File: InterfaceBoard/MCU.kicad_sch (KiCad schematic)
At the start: 6 parts, among them J1 Conn_ARM_JTAG_SWD_10, U4 STM32G0B1RET

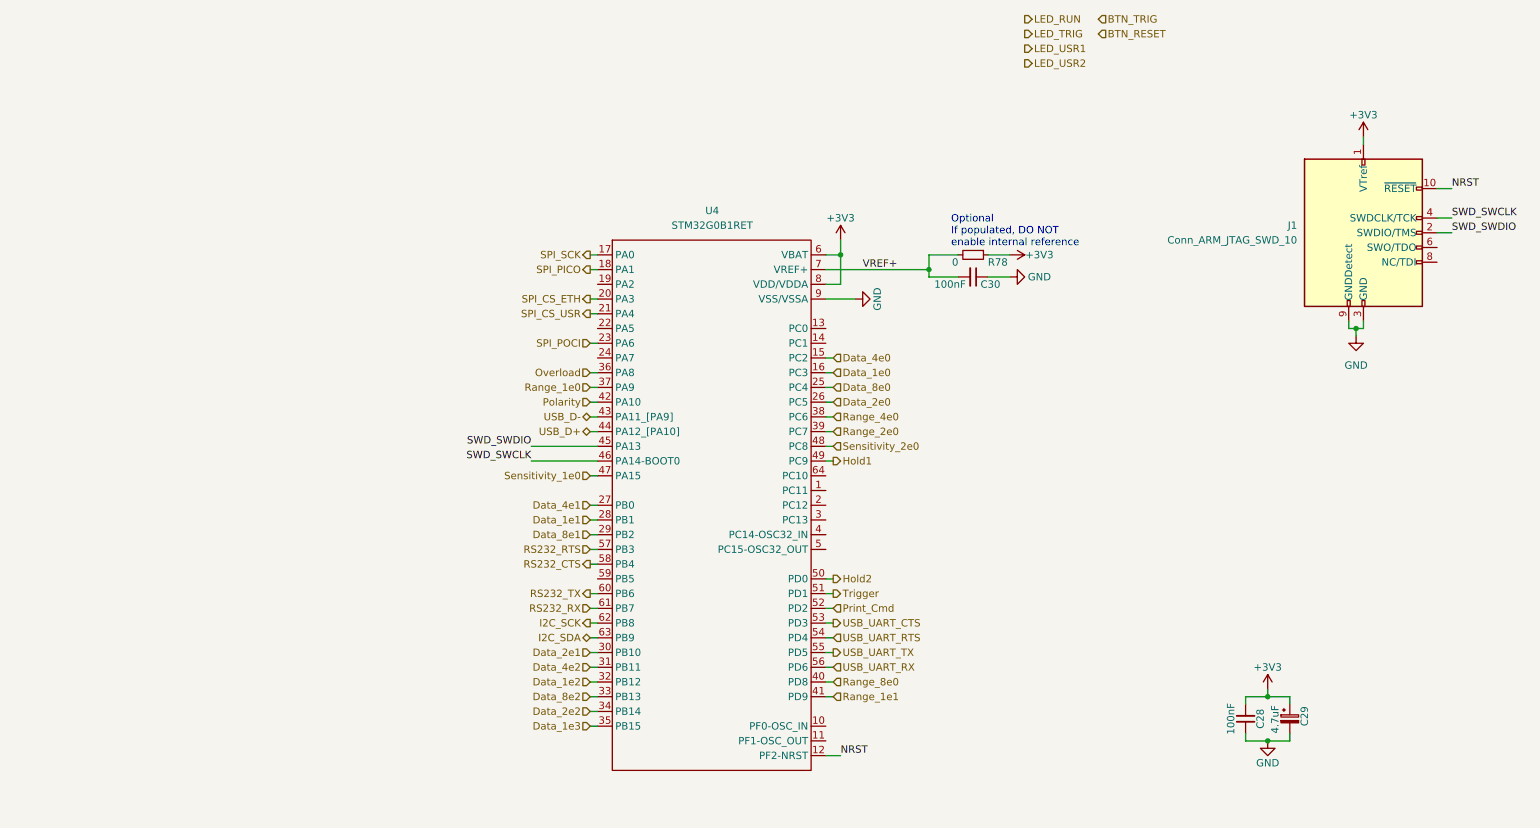
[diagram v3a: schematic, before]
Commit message: InterfaceBoard: Update connector footprint
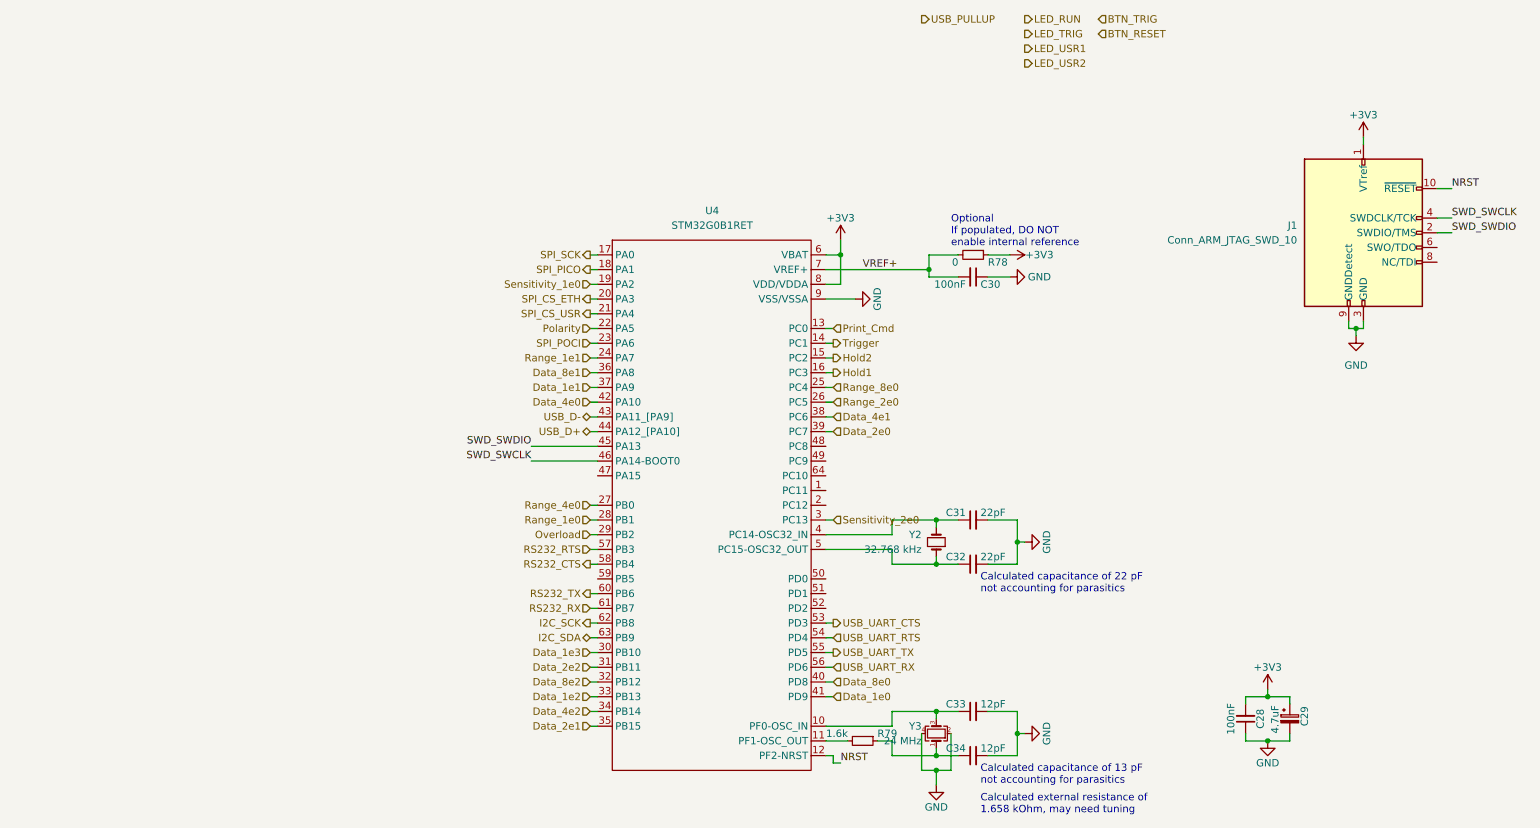
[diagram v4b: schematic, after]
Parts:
- added C31, C32: 22pF, Capacitor_SMD:C_0603_1608Metric, symbol Device:C_Small
- added C33, C34: 12pF, Capacitor_SMD:C_0603_1608Metric, symbol Device:C_Small
- added R79: 1.6k, Resistor_SMD:R_0603_1608Metric, symbol Device:R_Small
- added Y2: 32.768 kHz, Crystal:Crystal_C26-LF_D2.1mm_L6.5mm_Horizontal, symbol Device:Crystal_Small
- added Y3: 24 MHz, Crystal:Crystal_SMD_3225-4Pin_3.2x2.5mm, symbol Device:Crystal_GND24_Small
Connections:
- net Data_1e0: now also U4.41 (PD9); no longer U4.16 (PC3)
- net Data_1e1: now also U4.37 (PA9); no longer U4.28 (PB1)
- net Data_1e2: now also U4.33 (PB13); no longer U4.32 (PB12)
- net Data_1e3: now also U4.30 (PB10); no longer U4.35 (PB15)
- net Data_2e0: now also U4.39 (PC7); no longer U4.26 (PC5)
- net Data_2e1: now also U4.35 (PB15); no longer U4.30 (PB10)
- net Data_2e2: now also U4.31 (PB11); no longer U4.34 (PB14)
- net Data_4e0: now also U4.42 (PA10); no longer U4.15 (PC2)
- net Data_4e1: now also U4.38 (PC6); no longer U4.27 (PB0)
- net Data_4e2: now also U4.34 (PB14); no longer U4.31 (PB11)
- net Data_8e0: now also U4.40 (PD8); no longer U4.25 (PC4)
- net Data_8e1: now also U4.36 (PA8); no longer U4.29 (PB2)
- net Data_8e2: now also U4.32 (PB12); no longer U4.33 (PB13)
- net GND: now also C31.2, C32.2, C33.2, C34.2, Y3.2, Y3.4
- net Hold1: now also U4.16 (PC3); no longer U4.49 (PC9)
- net Hold2: now also U4.15 (PC2); no longer U4.50 (PD0)
- net Overload: now also U4.29 (PB2); no longer U4.36 (PA8)
- net Polarity: now also U4.22 (PA5); no longer U4.42 (PA10)
- net Print_Cmd: now also U4.13 (PC0); no longer U4.52 (PD2)
- net Range_1e0: now also U4.28 (PB1); no longer U4.37 (PA9)
- net Range_1e1: now also U4.24 (PA7); no longer U4.41 (PD9)
- net Range_2e0: now also U4.26 (PC5); no longer U4.39 (PC7)
- net Range_4e0: now also U4.27 (PB0); no longer U4.38 (PC6)
- net Range_8e0: now also U4.25 (PC4); no longer U4.40 (PD8)
- net Sensitivity_1e0: now also U4.19 (PA2); no longer U4.47 (PA15)
- net Sensitivity_2e0: now also U4.3 (PC13); no longer U4.48 (PC8)
- net Trigger: now also U4.14 (PC1); no longer U4.51 (PD1)
- net at U4.10 (PF0-OSC_IN): now also C33.1, Y3.3
- net at U4.11 (PF1-OSC_OUT): now also R79.2
- net at U4.4 (PC14-OSC32_IN): now also C31.1, Y2.2
- net at U4.5 (PC15-OSC32_OUT): now also C32.1, Y2.1
- new net: C34.1, R79.1, Y3.1
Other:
- note added: "Calculated capacitance of 13 pF not accounting for parasitics"
- note added: "Calculated capacitance of 22 pF not accounting for parasitics"
- note added: "Calculated external resistance of 1.658 kOhm, may need tuning"

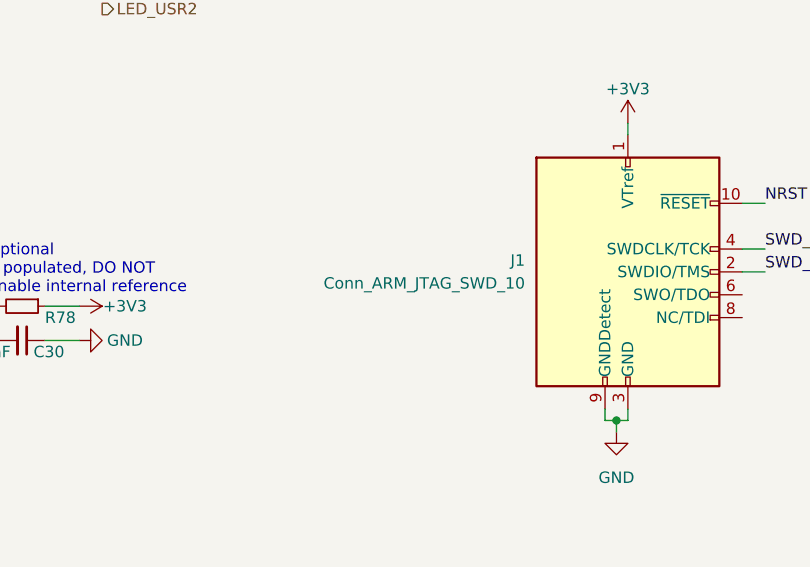
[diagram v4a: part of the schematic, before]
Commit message: InterfaceBoard: Add 3.3 V regulater, test points.
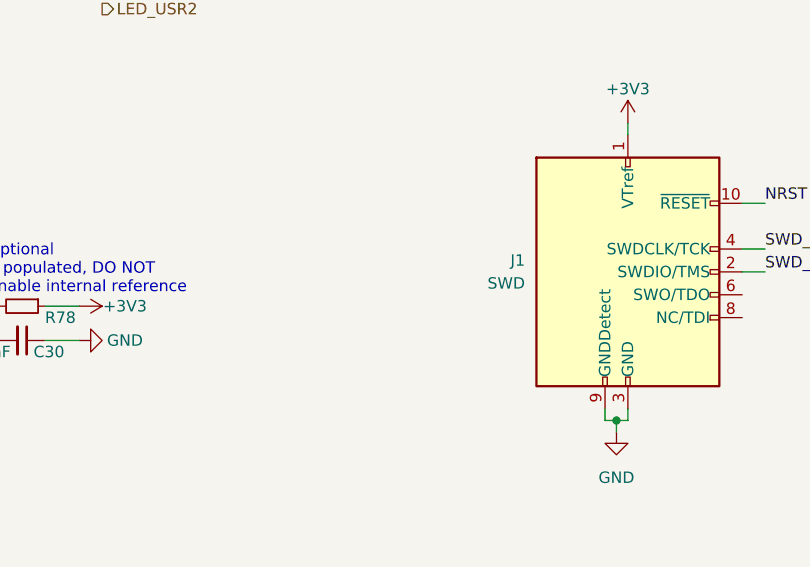
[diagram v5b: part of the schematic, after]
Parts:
- J1: value Conn_ARM_JTAG_SWD_10 -> SWD
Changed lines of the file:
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@@
       (effects (font (size 1.27 1.27)) (justify right))
     )
-    (property "Value" "Conn_ARM_JTAG_SWD_10" (id 1) (at 237.49 54.6099 0)
+    (property "Value" "SWD" (id 1) (at 237.49 54.6099 0)
       (effects (font (size 1.27 1.27)) (justify right))
     )

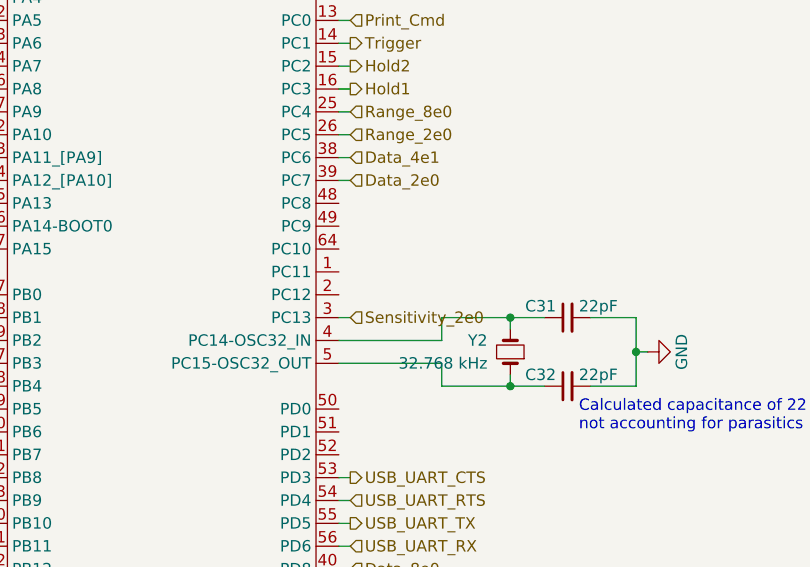
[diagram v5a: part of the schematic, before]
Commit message: InterfaceBoard: Routed some digital interfaces to MCU
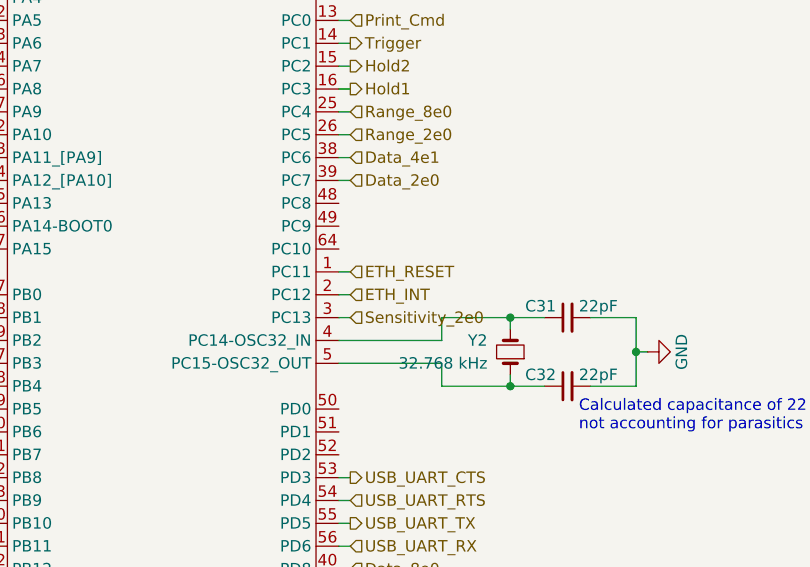
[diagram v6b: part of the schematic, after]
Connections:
- net ETH_RESET: now reaches U4.1 (PC11)
- net ETH_INT: now reaches U4.2 (PC12)
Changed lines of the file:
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@@
+    (stroke (width 0) (type default) (color 0 0 0 0))
+  )
+  (wire (pts (xy 156.21 100.33) (xy 157.48 100.33))
     (stroke (width 0) (type default) (color 0 0 0 0))
   )
@@
   )
   (wire (pts (xy 189.23 110.49) (xy 184.15 110.49))
+    (stroke (width 0) (type default) (color 0 0 0 0))
+  )
+  (wire (pts (xy 156.21 97.79) (xy 157.48 97.79))
     (stroke (width 0) (type default) (color 0 0 0 0))
   )
@@
     (effects (font (size 1.27 1.27)) (justify left))
   )
+  (hierarchical_label "ETH_RESET" (shape input) (at 157.48 97.79 0)
+    (effects (font (size 1.27 1.27)) (justify left))
+  )
   (hierarchical_label "Range_1e0" (shape input) (at 115.57 102.87 180)
     (effects (font (size 1.27 1.27)) (justify right))
@@
     (effects (font (size 1.27 1.27)) (justify left))
   )
+  (hierarchical_label "ETH_INT" (shape input) (at 157.48 100.33 0)
+    (effects (font (size 1.27 1.27)) (justify left))
+  )

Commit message: InterfaceBoard: Place and route buttons and LEDs.
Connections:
- net NRST is gone; now on net BTN_RESET: J1.10 (~{RESET}), U4.12 (PF2-NRST)
- net BTN_TRIG: now also U4.64 (PC10)
- net LED_RUN: now also U4.47 (PA15)
- net LED_TRIG: now also U4.48 (PC8)
- net LED_USR1: now also U4.49 (PC9)
- net LED_USR2: now also U4.50 (PD0)
- net USB_PULLUP: now also U4.59 (PB5)
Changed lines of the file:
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@@
   (junction (at 175.26 146.05) (diameter 0) (color 0 0 0 0)
   )
+  (junction (at 157.48 144.78) (diameter 0) (color 0 0 0 0)
+  )
   (junction (at 247.65 69.85) (diameter 0) (color 0 0 0 0)
   )
@@
     (stroke (width 0) (type default) (color 0 0 0 0))
   )
+  (wire (pts (xy 156.21 113.03) (xy 157.48 113.03))
+    (stroke (width 0) (type default) (color 0 0 0 0))
+  )
   (wire (pts (xy 105.41 90.17) (xy 116.84 90.17))
     (stroke (width 0) (type default) (color 0 0 0 0))
   )
+  (wire (pts (xy 115.57 113.03) (xy 116.84 113.03))
+    (stroke (width 0) (type default) (color 0 0 0 0))
+  )
   (wire (pts (xy 189.23 135.89) (xy 189.23 139.7))
     (stroke (width 0) (type default) (color 0 0 0 0))
@@
     (stroke (width 0) (type default) (color 0 0 0 0))
   )
+  (wire (pts (xy 156.21 95.25) (xy 157.48 95.25))
+    (stroke (width 0) (type default) (color 0 0 0 0))
+  )
   (wire (pts (xy 167.64 143.51) (xy 175.26 143.51))
     (stroke (width 0) (type default) (color 0 0 0 0))
@@
     (stroke (width 0) (type default) (color 0 0 0 0))
   )
+  (wire (pts (xy 158.75 147.32) (xy 157.48 147.32))
+    (stroke (width 0) (type default) (color 0 0 0 0))
+  )
   (wire (pts (xy 247.65 69.85) (xy 248.92 69.85))
     (stroke (width 0) (type default) (color 0 0 0 0))
@@
     (stroke (width 0) (type default) (color 0 0 0 0))
   )
+  (wire (pts (xy 156.21 90.17) (xy 157.48 90.17))
+    (stroke (width 0) (type default) (color 0 0 0 0))
+  )
+  (wire (pts (xy 115.57 95.25) (xy 116.84 95.25))
+    (stroke (width 0) (type default) (color 0 0 0 0))
+  )
   (wire (pts (xy 115.57 67.31) (xy 116.84 67.31))
     (stroke (width 0) (type default) (color 0 0 0 0))
@@
   )
   (wire (pts (xy 177.8 146.05) (xy 175.26 146.05))
+    (stroke (width 0) (type default) (color 0 0 0 0))
+  )
+  (wire (pts (xy 156.21 92.71) (xy 157.48 92.71))
+    (stroke (width 0) (type default) (color 0 0 0 0))
+  )
+  (wire (pts (xy 157.48 147.32) (xy 157.48 144.78))
     (stroke (width 0) (type default) (color 0 0 0 0))
   )
@@
     (effects (font (size 1.27 1.27)) (justify right))
   )
-  (hierarchical_label "LED_USR2" (shape output) (at 190.5 24.13 0)
+  (hierarchical_label "LED_USR2" (shape output) (at 157.48 113.03 0)
     (effects (font (size 1.27 1.27)) (justify left))
   )
@@
     (effects (font (size 1.27 1.27)) (justify left))
   )
-  (hierarchical_label "LED_RUN" (shape output) (at 190.5 16.51 0)
-    (effects (font (size 1.27 1.27)) (justify left))
+  (hierarchical_label "LED_RUN" (shape output) (at 115.57 95.25 180)
+    (effects (font (size 1.27 1.27)) (justify right))
   )
   (hierarchical_label "Data_1e3" (shape input) (at 115.57 125.73 180)
@@
     (effects (font (size 1.27 1.27)) (justify left))
   )
+  (hierarchical_label "USB_PULLUP" (shape output) (at 115.57 113.03 180)
+    (effects (font (size 1.27 1.27)) (justify right))
+  )
   (hierarchical_label "USB_UART_RX" (shape input) (at 157.48 128.27 0)
     (effects (font (size 1.27 1.27)) (justify left))
@@
     (effects (font (size 1.27 1.27)) (justify right))
   )
-  (hierarchical_label "USB_PULLUP" (shape output) (at 172.72 16.51 0)
-    (effects (font (size 1.27 1.27)) (justify left))
-  )
   (hierarchical_label "Data_1e0" (shape input) (at 157.48 133.35 0)
     (effects (font (size 1.27 1.27)) (justify left))
@@
     (effects (font (size 1.27 1.27)) (justify right))
   )
-  (hierarchical_label "BTN_TRIG" (shape input) (at 203.2 16.51 0)
+  (hierarchical_label "BTN_TRIG" (shape input) (at 157.48 95.25 0)
     (effects (font (size 1.27 1.27)) (justify left))
   )
@@
     (effects (font (size 1.27 1.27)) (justify right))
   )
-  (hierarchical_label "BTN_RESET" (shape input) (at 203.2 19.05 0)
+  (hierarchical_label "BTN_RESET" (shape input) (at 158.75 147.32 0)
     (effects (font (size 1.27 1.27)) (justify left))
   )
@@
     (effects (font (size 1.27 1.27)) (justify right))
   )
-  (hierarchical_label "LED_TRIG" (shape output) (at 190.5 19.05 0)
+  (hierarchical_label "LED_TRIG" (shape output) (at 157.48 90.17 0)
     (effects (font (size 1.27 1.27)) (justify left))
   )
@@
     (effects (font (size 1.27 1.27)) (justify right))
   )
-  (hierarchical_label "LED_USR1" (shape output) (at 190.5 21.59 0)
-    (effects (font (size 1.27 1.27)) (justify left))
-  )
+  (hierarchical_label "LED_USR1" (shape output) (at 157.48 92.71 0)
+    (effects (font (size 1.27 1.27)) (justify left))
+  )

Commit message: InterfaceBoard: Rev 1.0
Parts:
- renumbered C33 to C10, C29 to C11, C31 to C30, C32 to C31, C28 to C32, C30 to C33, C34 to C9, J1 to J4, R79 to R16, R78 to R86, U4 to U2, Y3 to Y2, Y2 to Y3
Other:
- company: (none) -> Peter Farley
- title: (none) -> Kiethley 615 Interface Board
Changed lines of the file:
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@@
 (kicad_sch (version 20211123) (generator eeschema)
   (paper "A4")
+  (title_block
+    (title "Kiethley 615 Interface Board")
+    (date "2023-03-04")
+    (rev "1.0")
+    (company "Peter Farley")
+    (comment 1 "Rev 1.0: Initial revision")
+  )
   (junction (at 189.23 106.68) (diameter 0) (color 0 0 0 0)
   )
@@
   (symbol (lib_id "Device:C_Small") (at 181.61 60.96 270) (mirror x) (unit 1)
     (in_bom yes) (on_board yes)
-    (property "Reference" "C30" (id 0) (at 182.88 62.23 90)
+    (property "Reference" "C33" (id 0) (at 182.88 62.23 90)
       (effects (font (size 1.27 1.27)) (justify left))
     )
@@
   (symbol (lib_id "Device:C_Small") (at 181.61 143.51 90) (unit 1)
     (in_bom yes) (on_board yes)
-    (property "Reference" "C34" (id 0) (at 180.34 142.24 90)
+    (property "Reference" "C9" (id 0) (at 180.34 142.24 90)
       (effects (font (size 1.27 1.27)) (justify left))
     )
@@
   (symbol (lib_id "Device:C_Small") (at 181.61 102.87 90) (unit 1)
     (in_bom yes) (on_board yes)
-    (property "Reference" "C31" (id 0) (at 180.34 101.6 90)
+    (property "Reference" "C30" (id 0) (at 180.34 101.6 90)
       (effects (font (size 1.27 1.27)) (justify left))
     )
@@
   (symbol (lib_id "Device:R_Small") (at 181.61 57.15 270) (unit 1)
     (in_bom yes) (on_board yes)
-    (property "Reference" "R78" (id 0) (at 184.15 58.42 90)
+    (property "Reference" "R86" (id 0) (at 184.15 58.42 90)
       (effects (font (size 1.27 1.27)) (justify left))
     )
@@
   (symbol (lib_id "Device:Crystal_Small") (at 175.26 106.68 90) (unit 1)
     (in_bom yes) (on_board yes)
-    (property "Reference" "Y2" (id 0) (at 172.72 105.41 90)
+    (property "Reference" "Y3" (id 0) (at 172.72 105.41 90)
       (effects (font (size 1.27 1.27)) (justify left))
     )
@@
   (symbol (lib_id "Device:R_Small") (at 162.56 140.97 270) (unit 1)
     (in_bom yes) (on_board yes)
-    (property "Reference" "R79" (id 0) (at 165.1 139.7 90)
+    (property "Reference" "R16" (id 0) (at 165.1 139.7 90)
       (effects (font (size 1.27 1.27)) (justify left))
     )
@@
   (symbol (lib_id "Device:C_Small") (at 228.6 137.16 0) (mirror x) (unit 1)
     (in_bom yes) (on_board yes)
-    (property "Reference" "C28" (id 0) (at 231.14 137.16 90))
+    (property "Reference" "C32" (id 0) (at 231.14 137.16 90))
     (property "Value" "100nF" (id 1) (at 226.06 137.16 90))
     (property "Footprint" "Capacitor_SMD:C_0603_1608Metric" (id 2) (at 228.6 137.16 0)
@@
   (symbol (lib_id "Connector:Conn_ARM_JTAG_SWD_10") (at 248.92 53.34 0) (unit 1)
     (in_bom yes) (on_board yes) (fields_autoplaced)
-    (property "Reference" "J1" (id 0) (at 237.49 52.0699 0)
+    (property "Reference" "J4" (id 0) (at 237.49 52.0699 0)
       (effects (font (size 1.27 1.27)) (justify right))
     )
@@
   (symbol (lib_id "Device:C_Polarized_Small") (at 236.22 137.16 0) (unit 1)
     (in_bom yes) (on_board yes)
-    (property "Reference" "C29" (id 0) (at 238.76 138.43 90)
+    (property "Reference" "C11" (id 0) (at 238.76 138.43 90)
       (effects (font (size 1.27 1.27)) (justify left))
     )
@@
   (symbol (lib_id "Device:Crystal_GND24_Small") (at 175.26 139.7 90) (unit 1)
     (in_bom yes) (on_board yes)
-    (property "Reference" "Y3" (id 0) (at 172.72 138.43 90)
+    (property "Reference" "Y2" (id 0) (at 172.72 138.43 90)
       (effects (font (size 1.27 1.27)) (justify left))
     )
@@
   (symbol (lib_id "lib_symbols:STM32G0B1RET") (at 137.16 54.61 0) (unit 1)
     (in_bom yes) (on_board yes) (fields_autoplaced)
-    (property "Reference" "U4" (id 0) (at 136.6084 49.53 0))
+    (property "Reference" "U2" (id 0) (at 136.6084 49.53 0))
     (property "Value" "STM32G0B1RET" (id 1) (at 136.6084 52.07 0))
     (property "Footprint" "Package_QFP:LQFP-64_10x10mm_P0.5mm" (id 2) (at 130.81 54.61 0)
@@
   (symbol (lib_id "Device:C_Small") (at 181.61 135.89 90) (unit 1)
     (in_bom yes) (on_board yes)
-    (property "Reference" "C33" (id 0) (at 180.34 134.62 90)
+    (property "Reference" "C10" (id 0) (at 180.34 134.62 90)
       (effects (font (size 1.27 1.27)) (justify left))
     )
@@
   (symbol (lib_id "Device:C_Small") (at 181.61 110.49 90) (unit 1)
     (in_bom yes) (on_board yes)
-    (property "Reference" "C32" (id 0) (at 180.34 109.22 90)
-      (effects (font (size 1.27 1.27)) (justify left))
-    )
+    (property "Reference" "C31" (id 0) (at 180.34 109.22 90)
+      (effects (font (size 1.27 1.27)) (justify left))
+    )
